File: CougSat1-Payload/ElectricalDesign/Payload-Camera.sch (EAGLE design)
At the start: 74 parts, among them J1 CougSat Card, U1 AD7291, U10 TXS0102DQM, U11 TXS0102DQM, U12 TXS0102DQM, U13 TXS0102DQM, U14 TXS0102DQM, U15 TXS0102DQM, U2 AD8515, U3 AD8616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

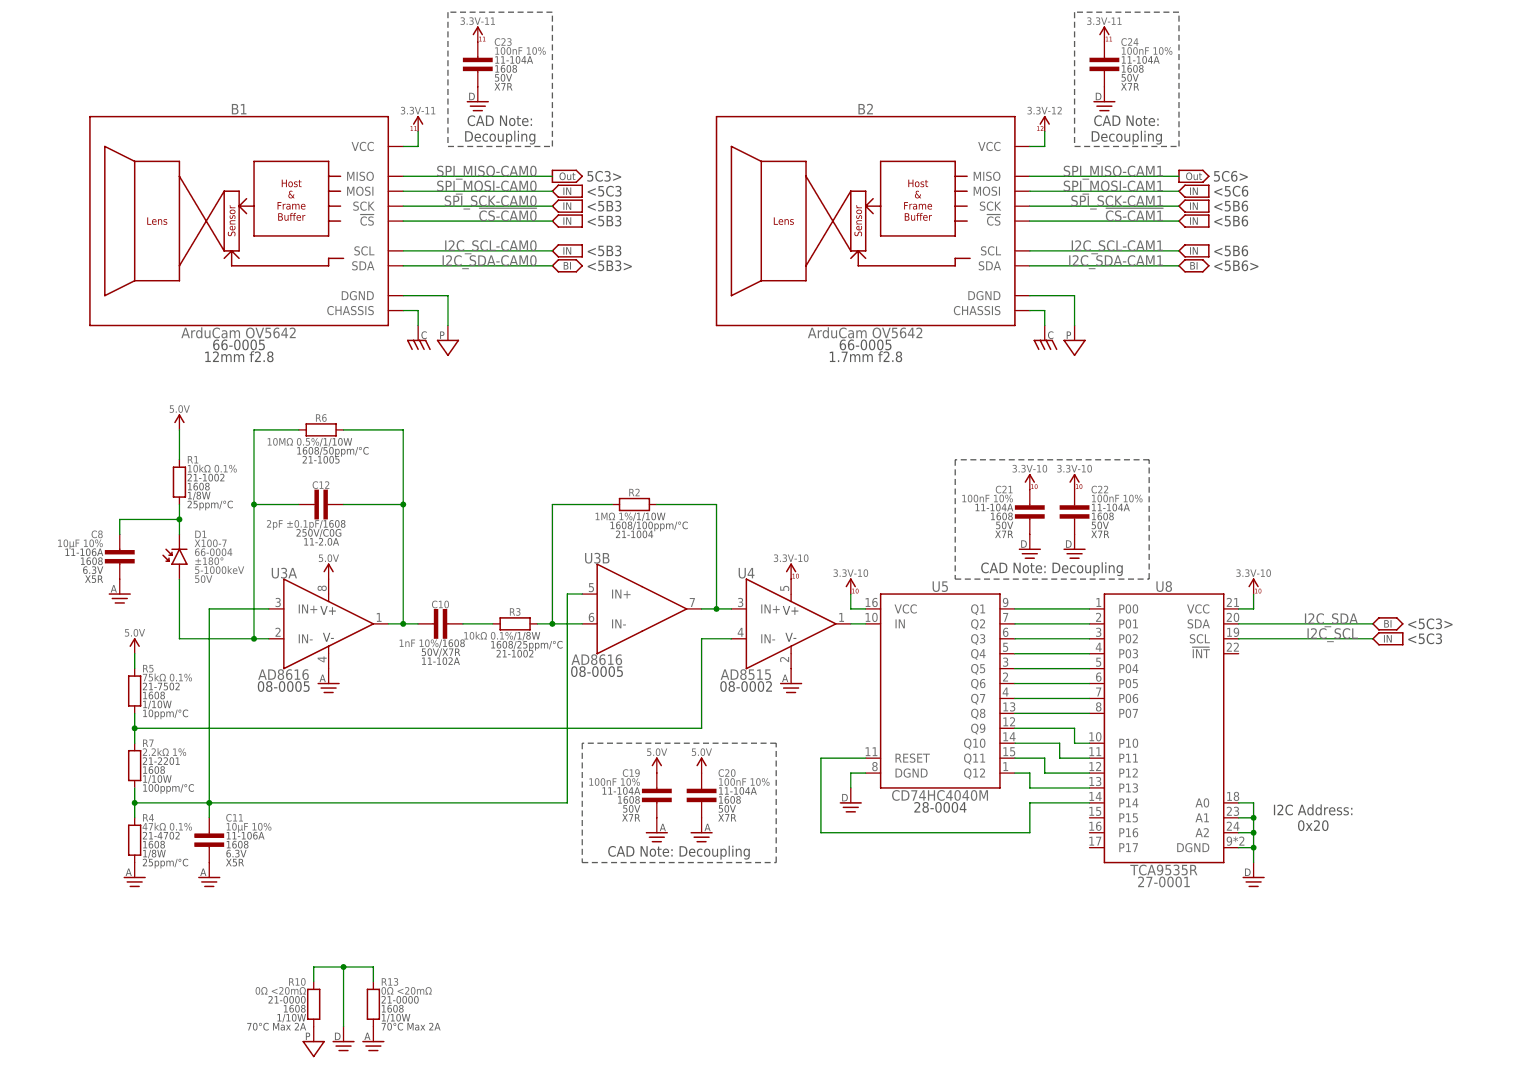
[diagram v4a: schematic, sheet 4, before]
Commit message: Minor schematic changes
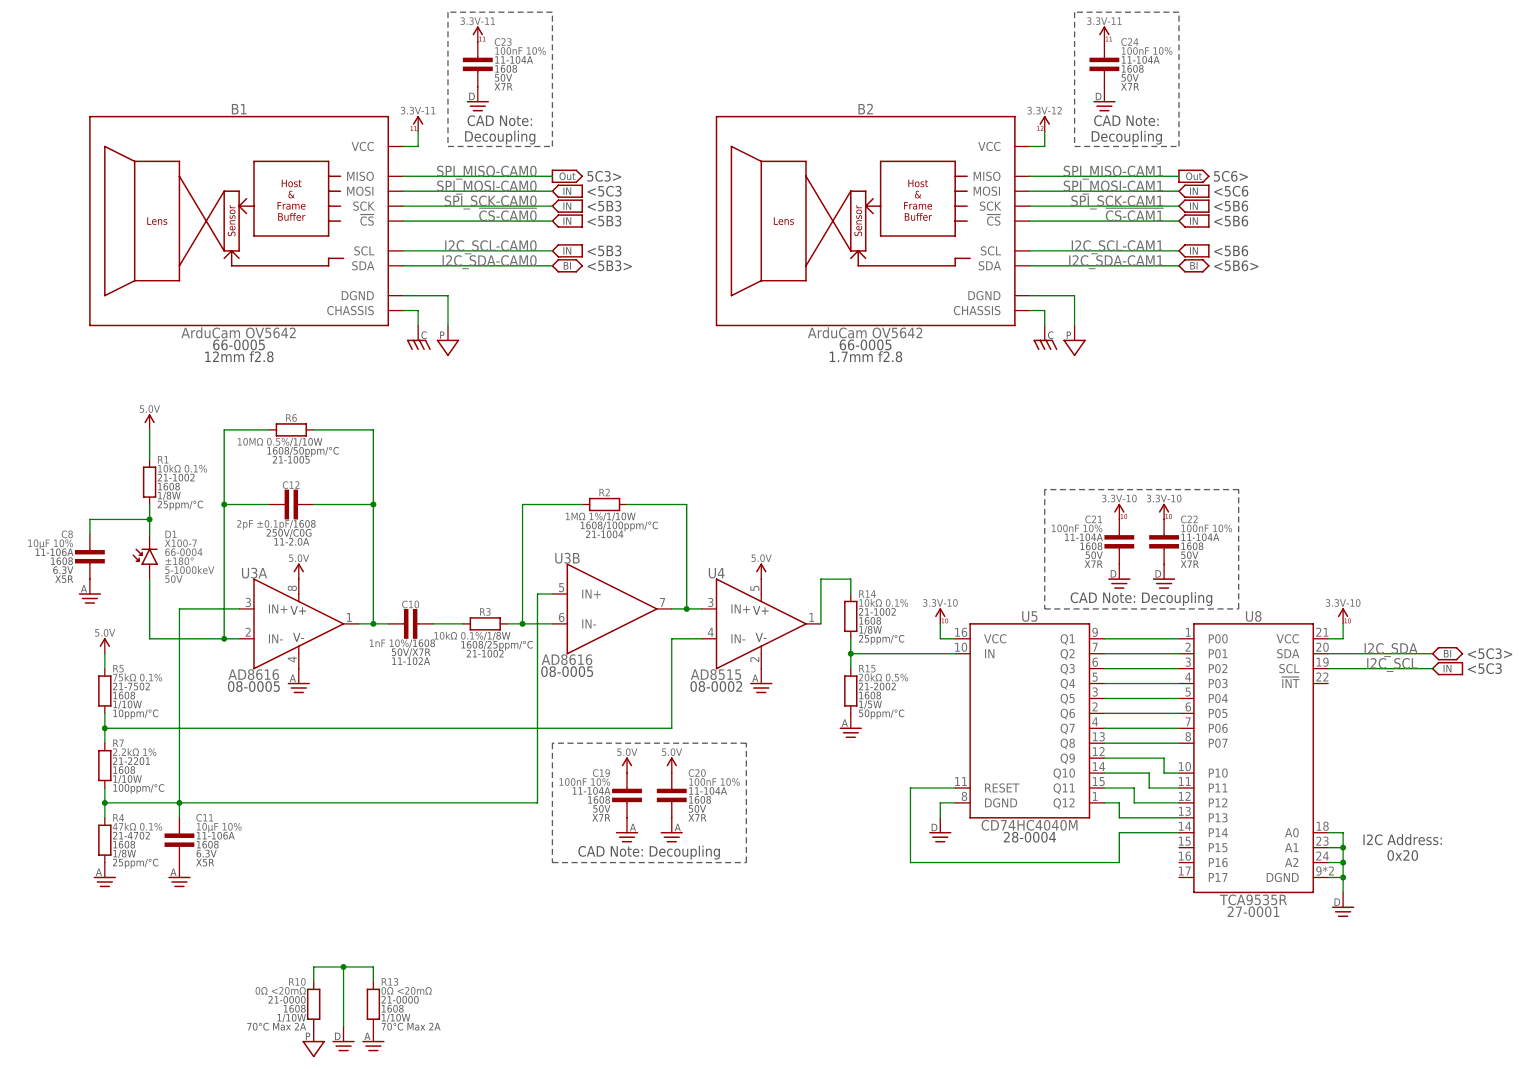
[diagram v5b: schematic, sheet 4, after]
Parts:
- added R14: 10kΩ 0.1%, CougsInSpace-Resistors:RES-V-10K-1608
- added R15: 20kΩ 0.5%, CougsInSpace-Resistors:RES-V-20K-1608
- added TP6, TP7: TEST_POINT-THT-1.0, CougsInSpace-Connectors:TEST_POINT-THT-1.0
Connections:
- removed net PD_OUTD: U4.OUT, U5.IN
- new net COUNTER_IN: R14.1, R15.2, U5.IN
- new net SENSOR_OUT: R14.2, U4.OUT
- net 3.3V_0: now also J1POWER.PR_3.3V-0
- net 3.3V_10: no longer U4.V+
- net 5.0V: now also TP7.1, U4.V+
- net AGND: now also R15.1
- net PGND: now also TP6.1
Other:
- note added: "Page 1: Block Diagram Page 2: Power Rails Page 3: Connector/ADC Page 4: Particle Counter, Cameras Page 5: Buffers Page 6: Mechanical"
- note removed: "Page 1: Block Diagram Page 2: Power Rails Page 3: Connector/ADC Page 4: Geiger Counter, Cameras Page 4: Mechanical"
- moved on the sheet: C10, C11, C12, C13, C14, C15, C17, C18, C19, C20, C21, C22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

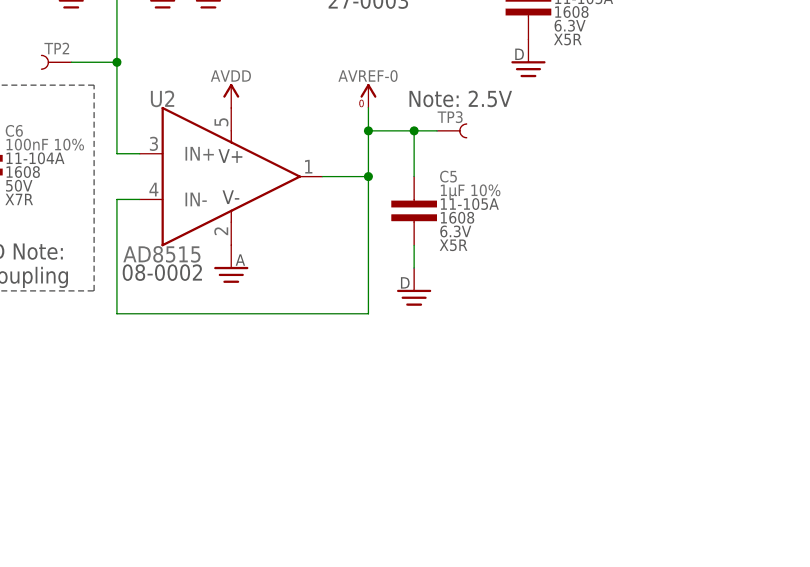
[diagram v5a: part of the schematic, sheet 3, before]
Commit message: Switched a DGND to AGND
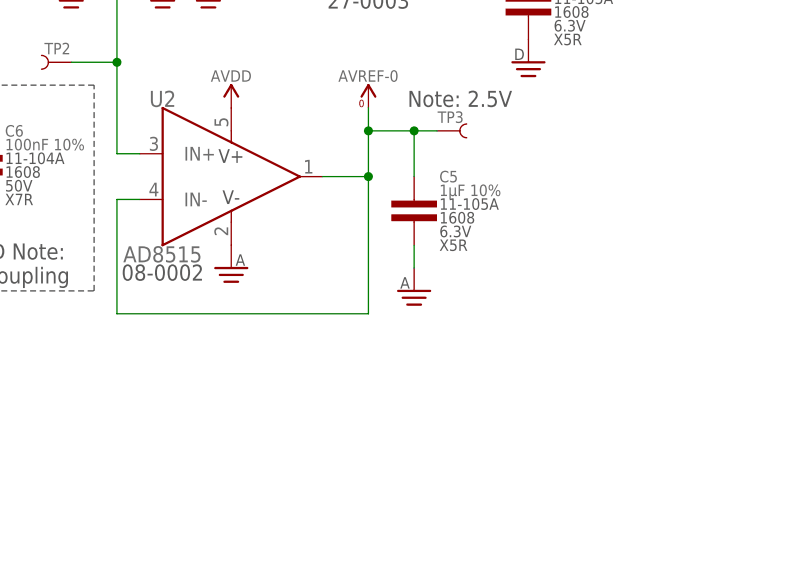
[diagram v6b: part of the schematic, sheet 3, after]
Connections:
- net AGND: now also C5.2
- net DGND: no longer C5.2
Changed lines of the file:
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@@
 <part name="RT8" library="CougsInSpace-Resistors" deviceset="THERMISTOR-V" device="-1608" technology="-10K" value="10kΩ 5%"/>
 <part name="C5" library="CougsInSpace-Capacitors" deviceset="CAP-V" device="-1608" technology="-1UF" value="1µF 10%"/>
-<part name="SUPPLY21" library="CougsInSpace-PowerSymbols" deviceset="DGND" device=""/>
 <part name="TP3" library="CougsInSpace-Connectors" deviceset="TEST_POINT" device="-SMD-C-1.25"/>
 <part name="C6" library="CougsInSpace-Capacitors" deviceset="CAP-V" device="-1608" technology="-100NF" value="100nF 10%"/>
@@
 <part name="R15" library="CougsInSpace-Resistors" deviceset="RES-V" device="-1608" technology="-20K" value="20kΩ 0.5%"/>
 <part name="SUPPLY96" library="CougsInSpace-PowerSymbols" deviceset="AGND" device=""/>
+<part name="SUPPLY21" library="CougsInSpace-PowerSymbols" deviceset="AGND" device=""/>
 </parts>
 <sheets>
@@
 <attribute name="TEMP" x="200.914" y="40.64" size="1.27" layer="97" align="center-left"/>
 </instance>
-<instance part="SUPPLY21" gate="1" x="198.12" y="35.56" smashed="yes"/>
 <instance part="TP3" gate="G$1" x="200.66" y="53.34" smashed="yes" rot="MR0">
 <attribute name="NAME" x="202.184" y="54.864" size="1.27" layer="95" rot="MR0" align="center"/>
@@
 <attribute name="NAME" x="254.254" y="165.1" size="1.27" layer="95" rot="MR0" align="center"/>
 </instance>
+<instance part="SUPPLY21" gate="G$1" x="198.12" y="35.56" smashed="yes"/>
 </instances>
 <busses>
@@
 <pinref part="C7" gate="G$1" pin="2"/>
 </segment>
+<segment>
+<pinref part="C5" gate="G$1" pin="2"/>
+<wire x1="198.12" y1="38.1" x2="198.12" y2="40.64" width="0.1524" layer="91"/>
+<pinref part="SUPPLY21" gate="G$1" pin="AGND"/>
+</segment>
 </net>
 <net name="AVDD" class="0">
@@
 </segment>
 <segment>
-<pinref part="SUPPLY21" gate="1" pin="DGND"/>
-<pinref part="C5" gate="G$1" pin="2"/>
-<wire x1="198.12" y1="38.1" x2="198.12" y2="40.64" width="0.1524" layer="91"/>
-</segment>
-<segment>

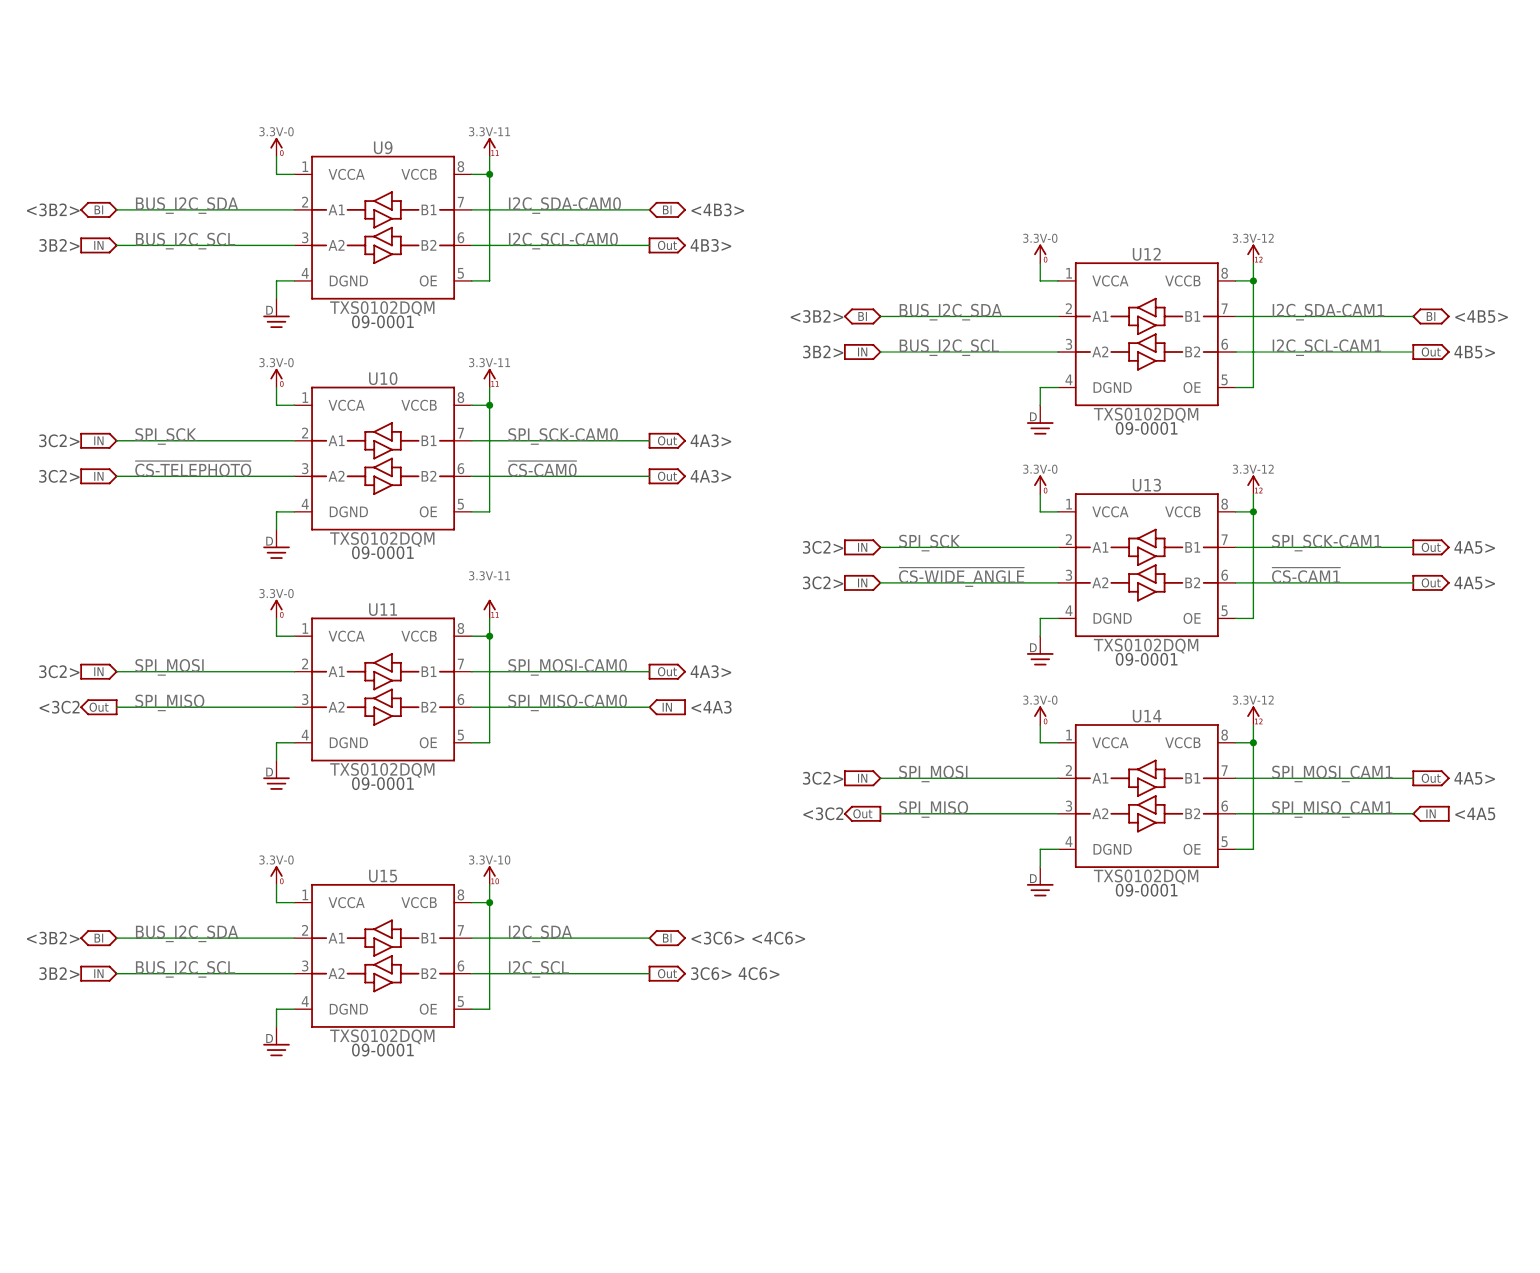
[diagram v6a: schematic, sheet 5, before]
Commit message: Added dcaps to buffers, specified 7b I2C addresses
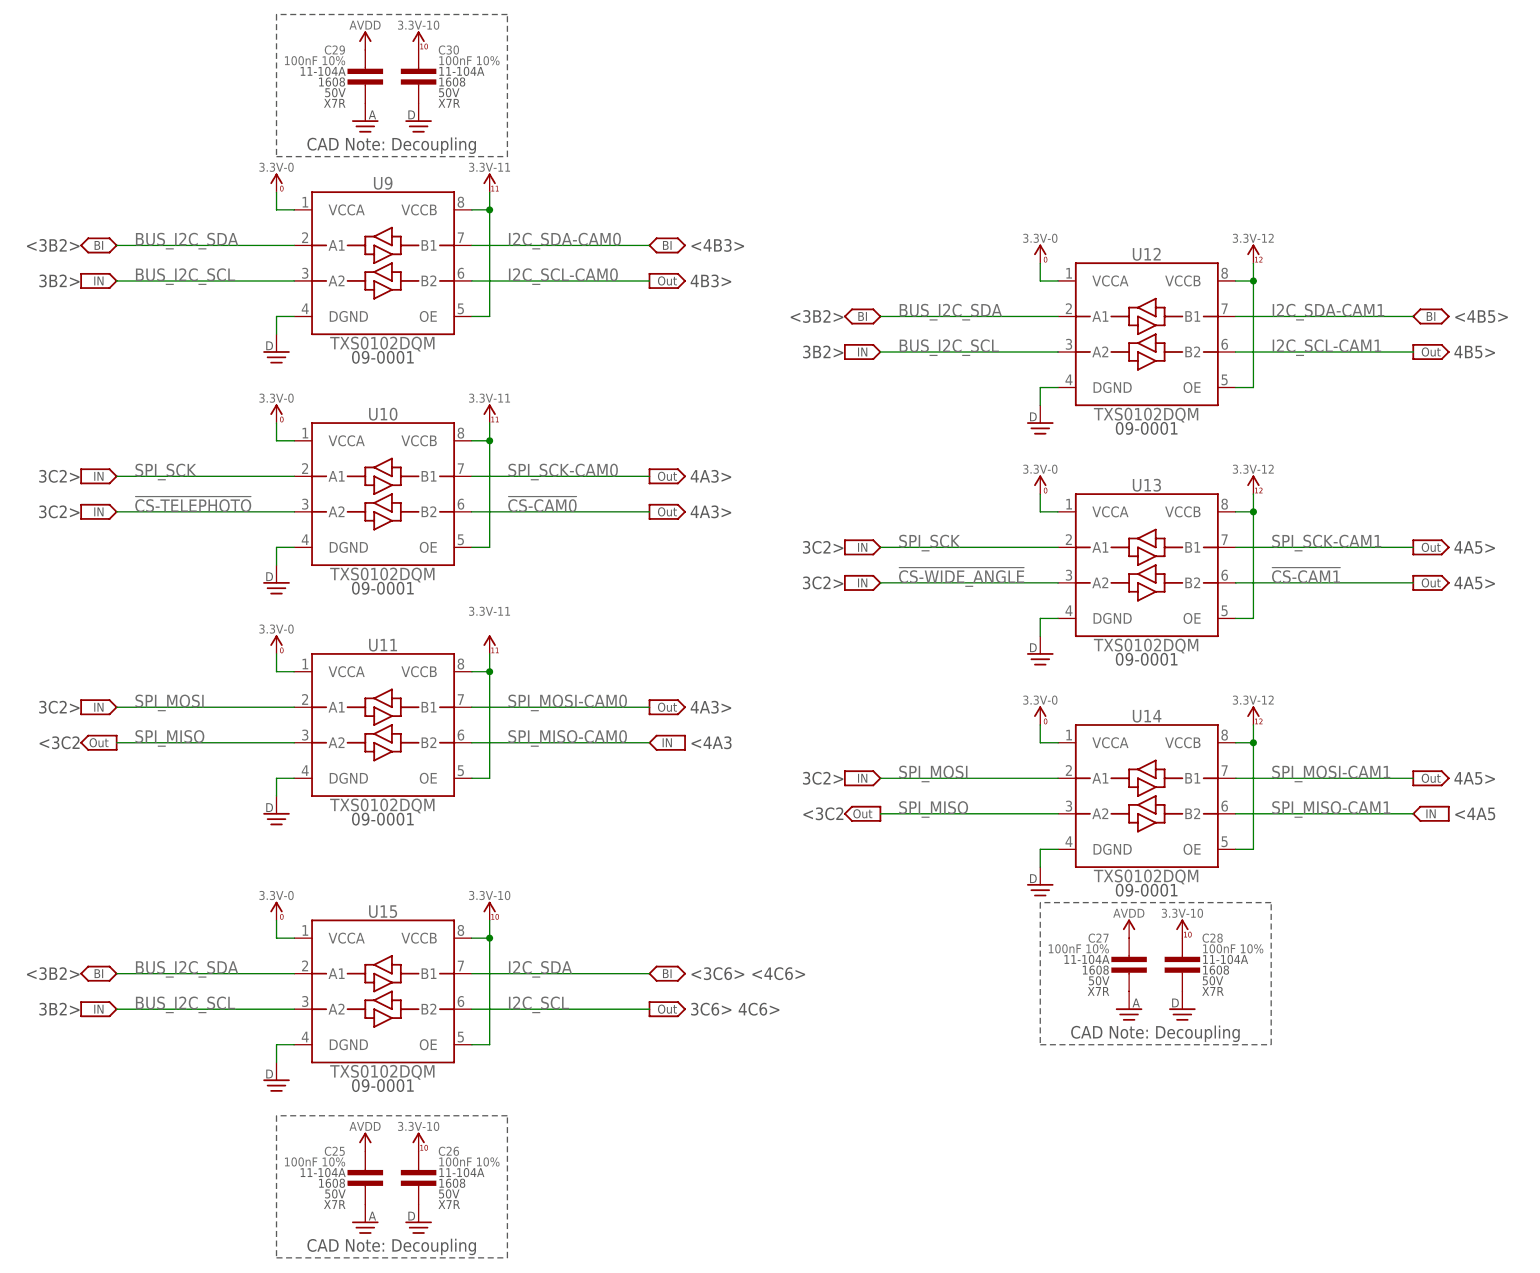
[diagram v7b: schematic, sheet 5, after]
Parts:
- added C25, C26, C27, C28, C29, C30: 100nF 10%, CougsInSpace-Capacitors:CAP-V-100NF-1608
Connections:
- removed net SPI_MISO_CAM1: U14.B2
- removed net SPI_MOSI_CAM1: U14.B1
- net 3.3V_10: now also C26.1, C28.1, C30.1
- net AGND: now also C25.2, C27.2, C29.2
- net AVDD: now also C25.1, C27.1, C29.1
- net DGND: now also C26.2, C28.2, C30.2
- net SPI_MISO-CAM1: now also U14.B2
- net SPI_MOSI-CAM1: now also U14.B1
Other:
- note added: "I2C Address: 0x20 (7b)"
- note added: "I2C Address: 0x22 (7b)"
- note removed: "I2C Address: 0x20"
- note removed: "I2C Address: 0x22"
- moved on the sheet: U10, U11, U15, U9

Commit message: Placed components
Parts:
- removed J1: CougSat Card, CougsInSpace-Boards:CIS_CARD
- added J2: CougSat Card, CougsInSpace-Boards:CIS_CARD-OPEN+X
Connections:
- net !CS-TELEPHOTO: now also J2GPIO.GPIO-0; no longer J1GPIO.GPIO-0
- net !CS-WIDE_ANGLE: now also J2GPIO.GPIO-1; no longer J1GPIO.GPIO-1
- net 3.3V_0: now also C25.1, C27.1, C29.1, J2POWER.PR_3.3V-0; no longer J1POWER.PR_3.3V-0
- net 3.3V_10: now also J2POWER.PR_3.3V-10; no longer J1POWER.PR_3.3V-10
- net 3.3V_11: now also J2POWER.PR_3.3V-11; no longer C24.1, J1POWER.PR_3.3V-11
- net 3.3V_12: now also C24.1, J2POWER.PR_3.3V-12; no longer J1POWER.PR_3.3V-12
- net AGND: now also RT1.1, RT2.1, RT3.1, RT4.1, RT5.1, RT6.1, RT7.1, RT8.1; no longer C25.2, C27.2, C29.2
- net AVDD: no longer C25.1, C27.1, C29.1
- net BUS_I2C_SCL: now also J2DATA.BUS_I2C1_SCL; no longer J1DATA.BUS_I2C1_SCL
- net BUS_I2C_SDA: now also J2DATA.BUS_I2C1_SDA; no longer J1DATA.BUS_I2C1_SDA
- net CHASSIS: now also J2POWER.CHASSIS; no longer J1POWER.CHASSIS
- net DGND: now also C25.2, C27.2, C29.2, U8.P15, U8.P16, U8.P17; no longer C23.2, C24.2, RT1.1, RT2.1, RT3.1, RT4.1, RT5.1, RT6.1, RT7.1, RT8.1
- net PGND: now also C23.2, C24.2, J2POWER.PGND; no longer J1POWER.PGND
- net SPI_MISO: now also J2DATA.BUS_SPI_MISO; no longer J1DATA.BUS_SPI_MISO
- net SPI_MOSI: now also J2DATA.BUS_SPI_MOSI; no longer J1DATA.BUS_SPI_MOSI
- net SPI_SCK: now also J2DATA.BUS_SPI_SCK; no longer J1DATA.BUS_SPI_SCK
